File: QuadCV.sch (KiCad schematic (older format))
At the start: 22 parts, among them U8 MCP6004

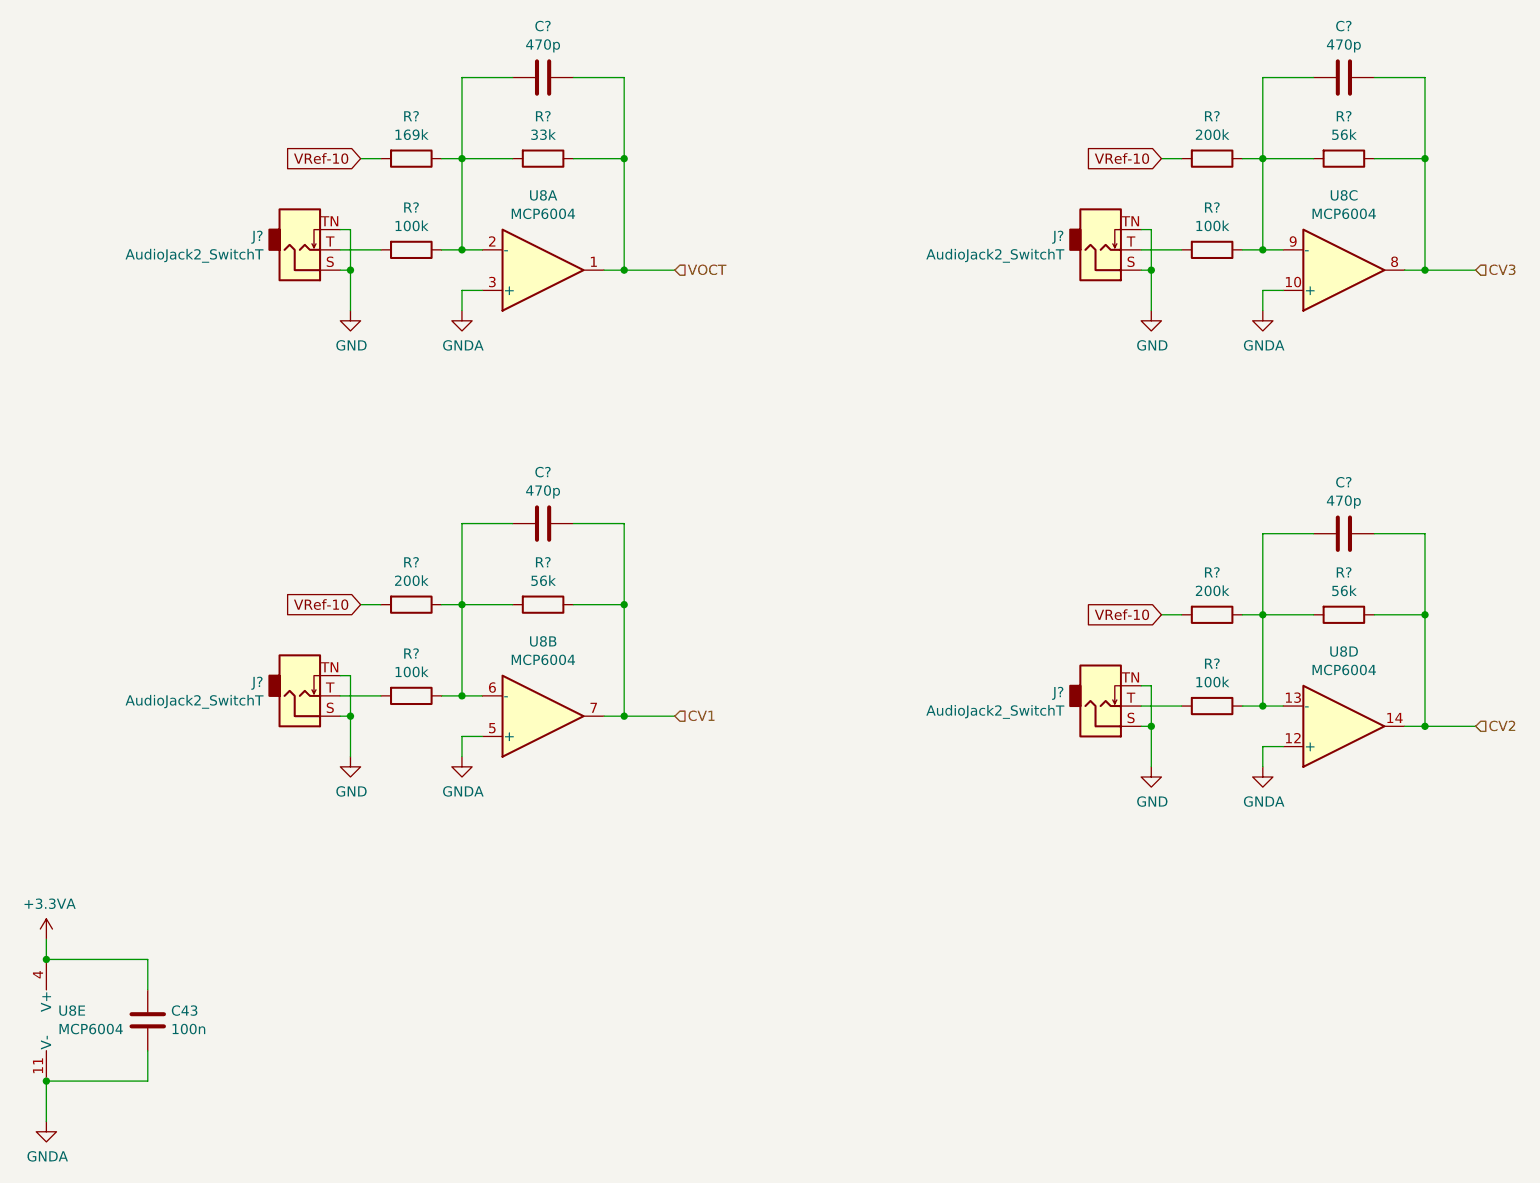
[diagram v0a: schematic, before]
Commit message: Added UI components.
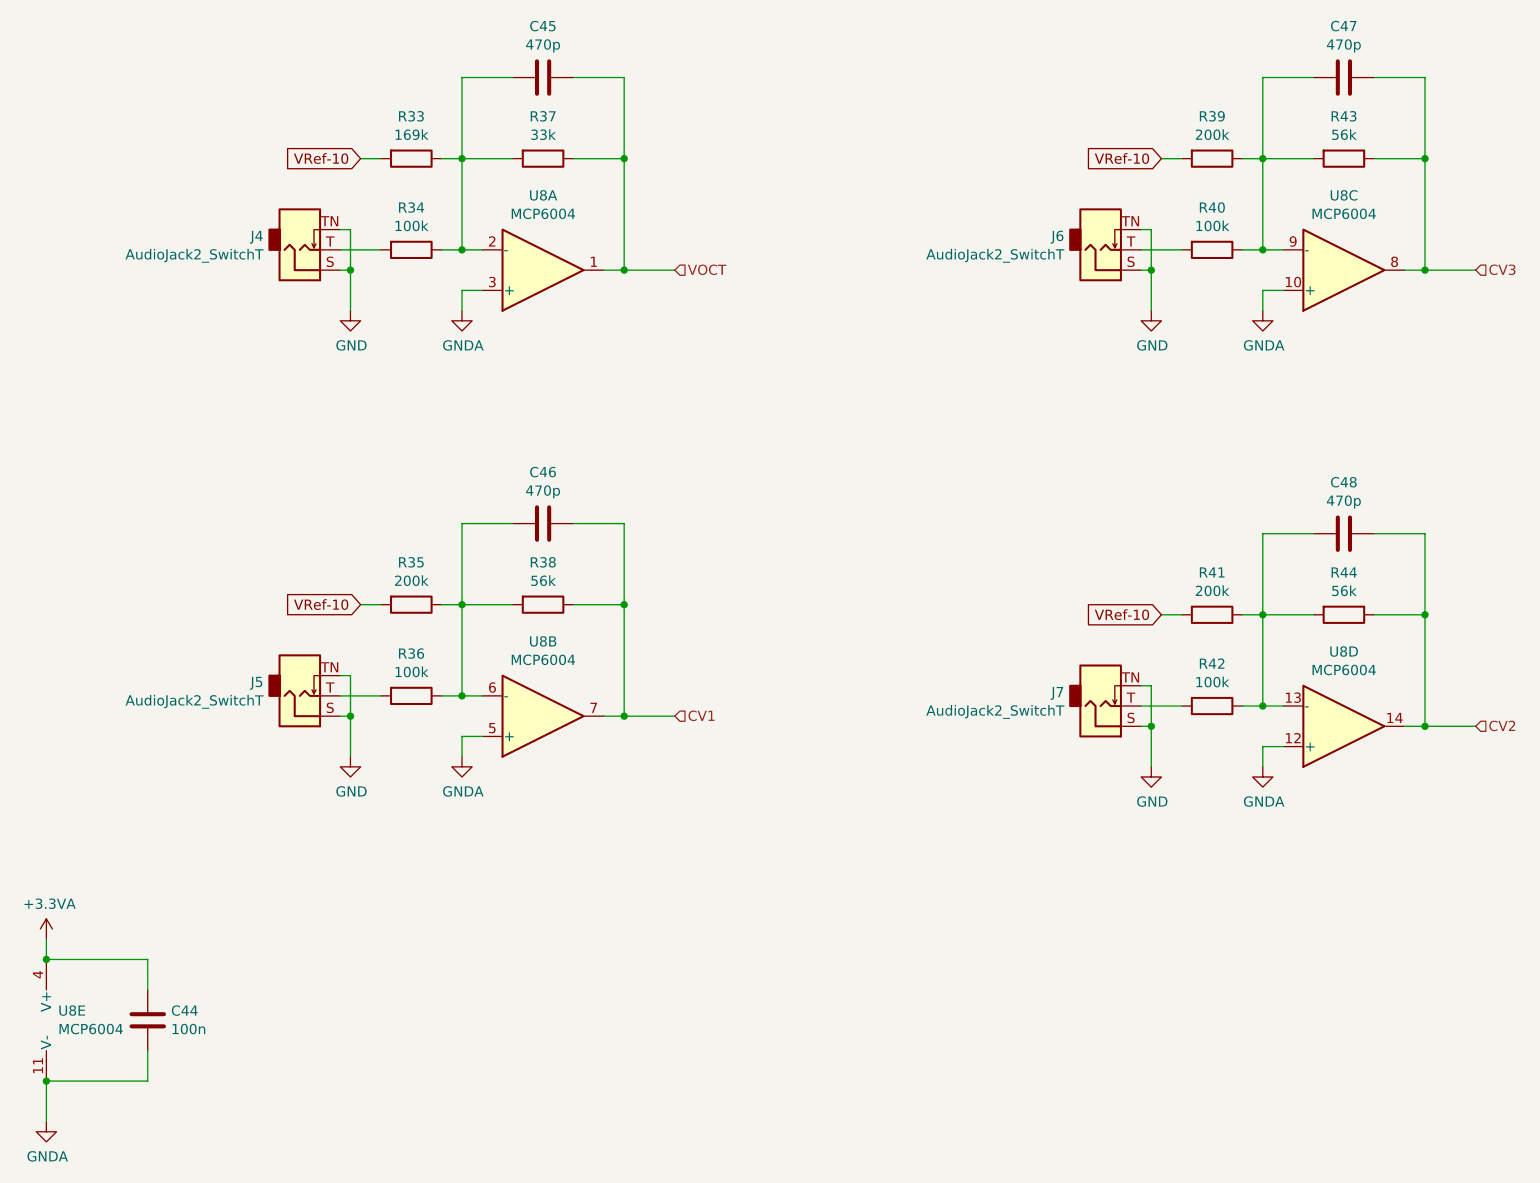
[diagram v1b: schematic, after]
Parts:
- gave numbers to parts that had none: 4
- renumbered C43 to C44, C44 to C45, C45 to C46, C46 to C47, C47 to C48, R27 to R33, R28 to R34, R29 to R35, R30 to R36, R31 to R37, R32 to R38, R33 to R39, R34 to R40, R35 to R41, R36 to R42, R37 to R43, R38 to R44

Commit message: Moved codec to audio module.
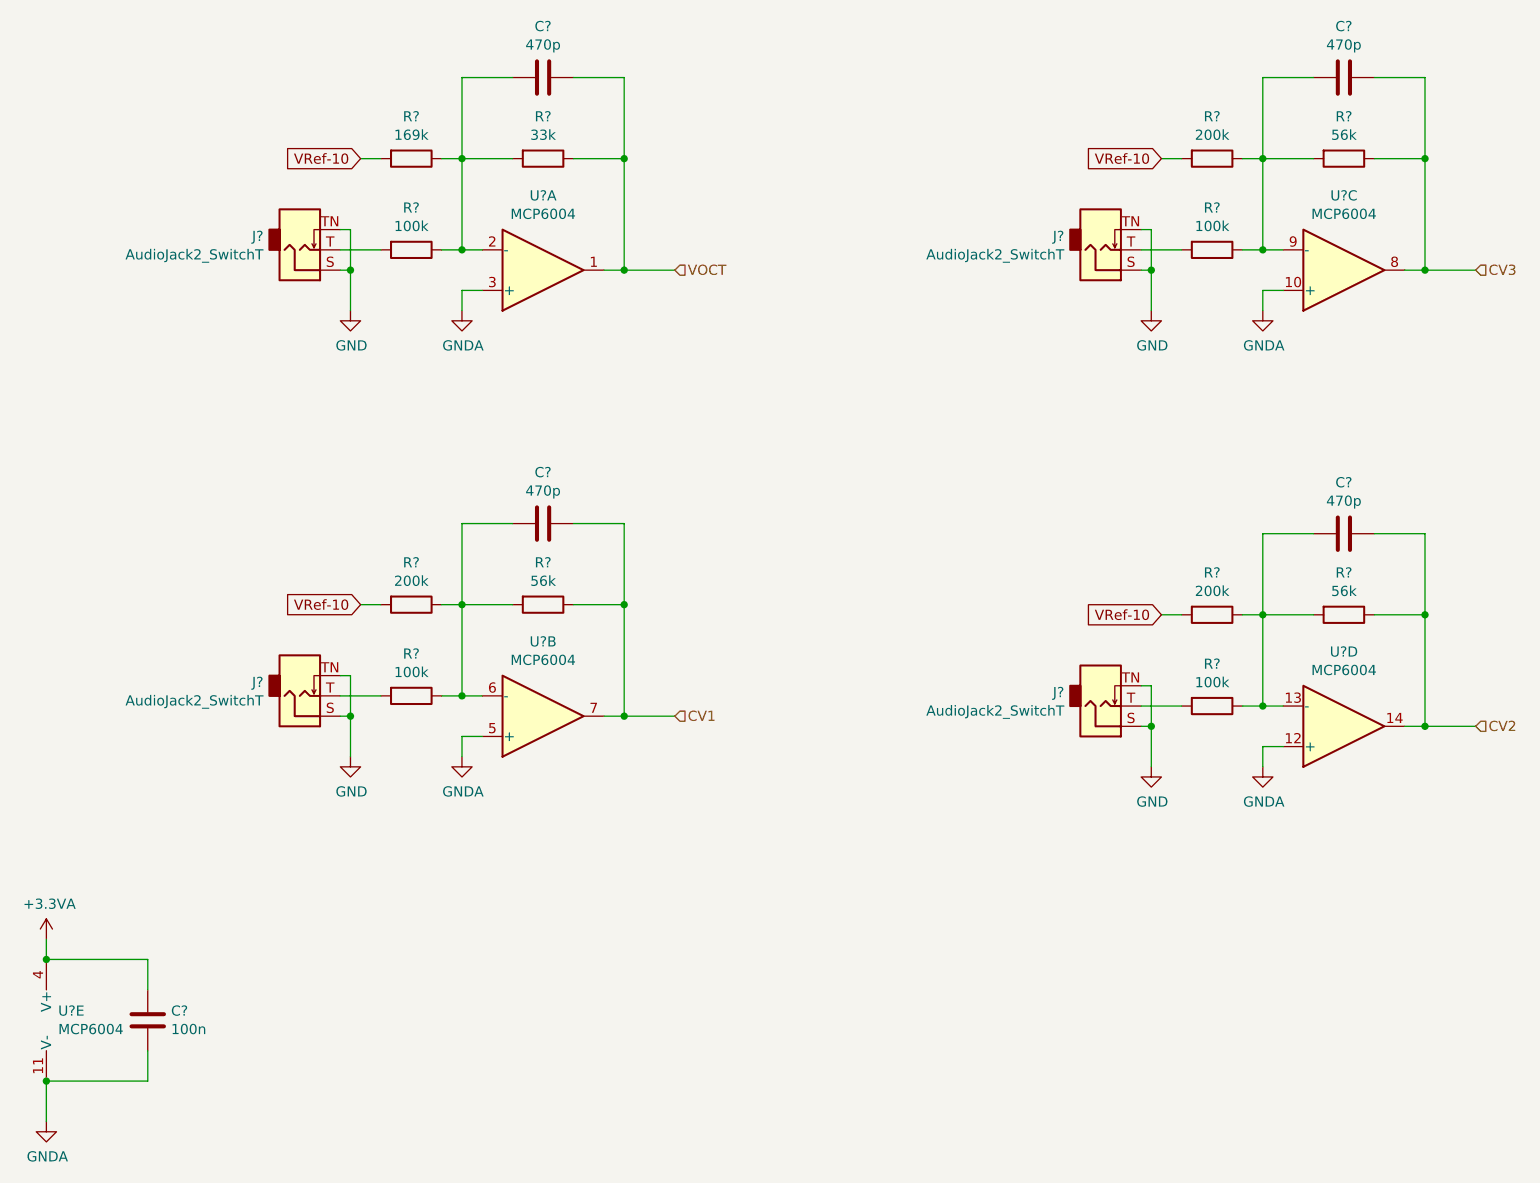
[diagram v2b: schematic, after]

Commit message: Re-annotation.
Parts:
- renumbered C44 to C27, C45 to C28, C46 to C29, C47 to C30, C48 to C31, R33 to R13, R34 to R14, R35 to R15, R36 to R16, R37 to R17, R38 to R18, R39 to R19, R40 to R20, R41 to R21, R42 to R22, R43 to R23, R44 to R24, U8 to U6

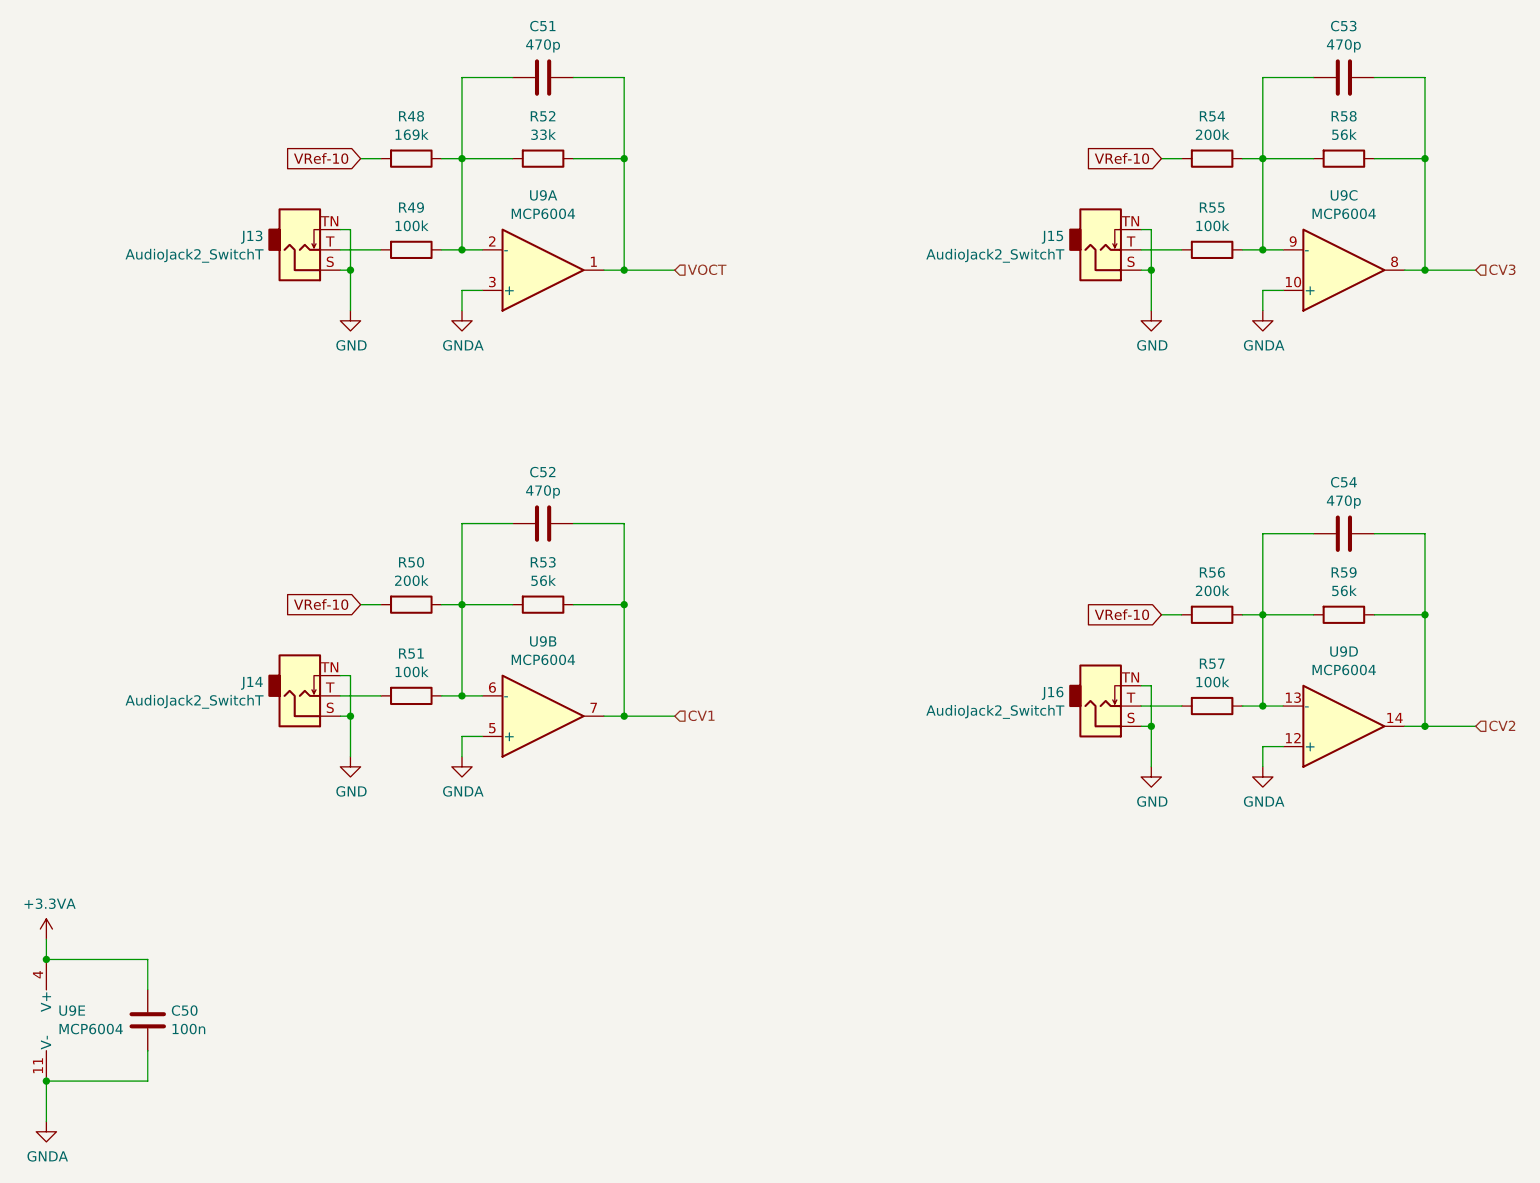
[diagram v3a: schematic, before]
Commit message: Assigned pins and cleared schema rules.
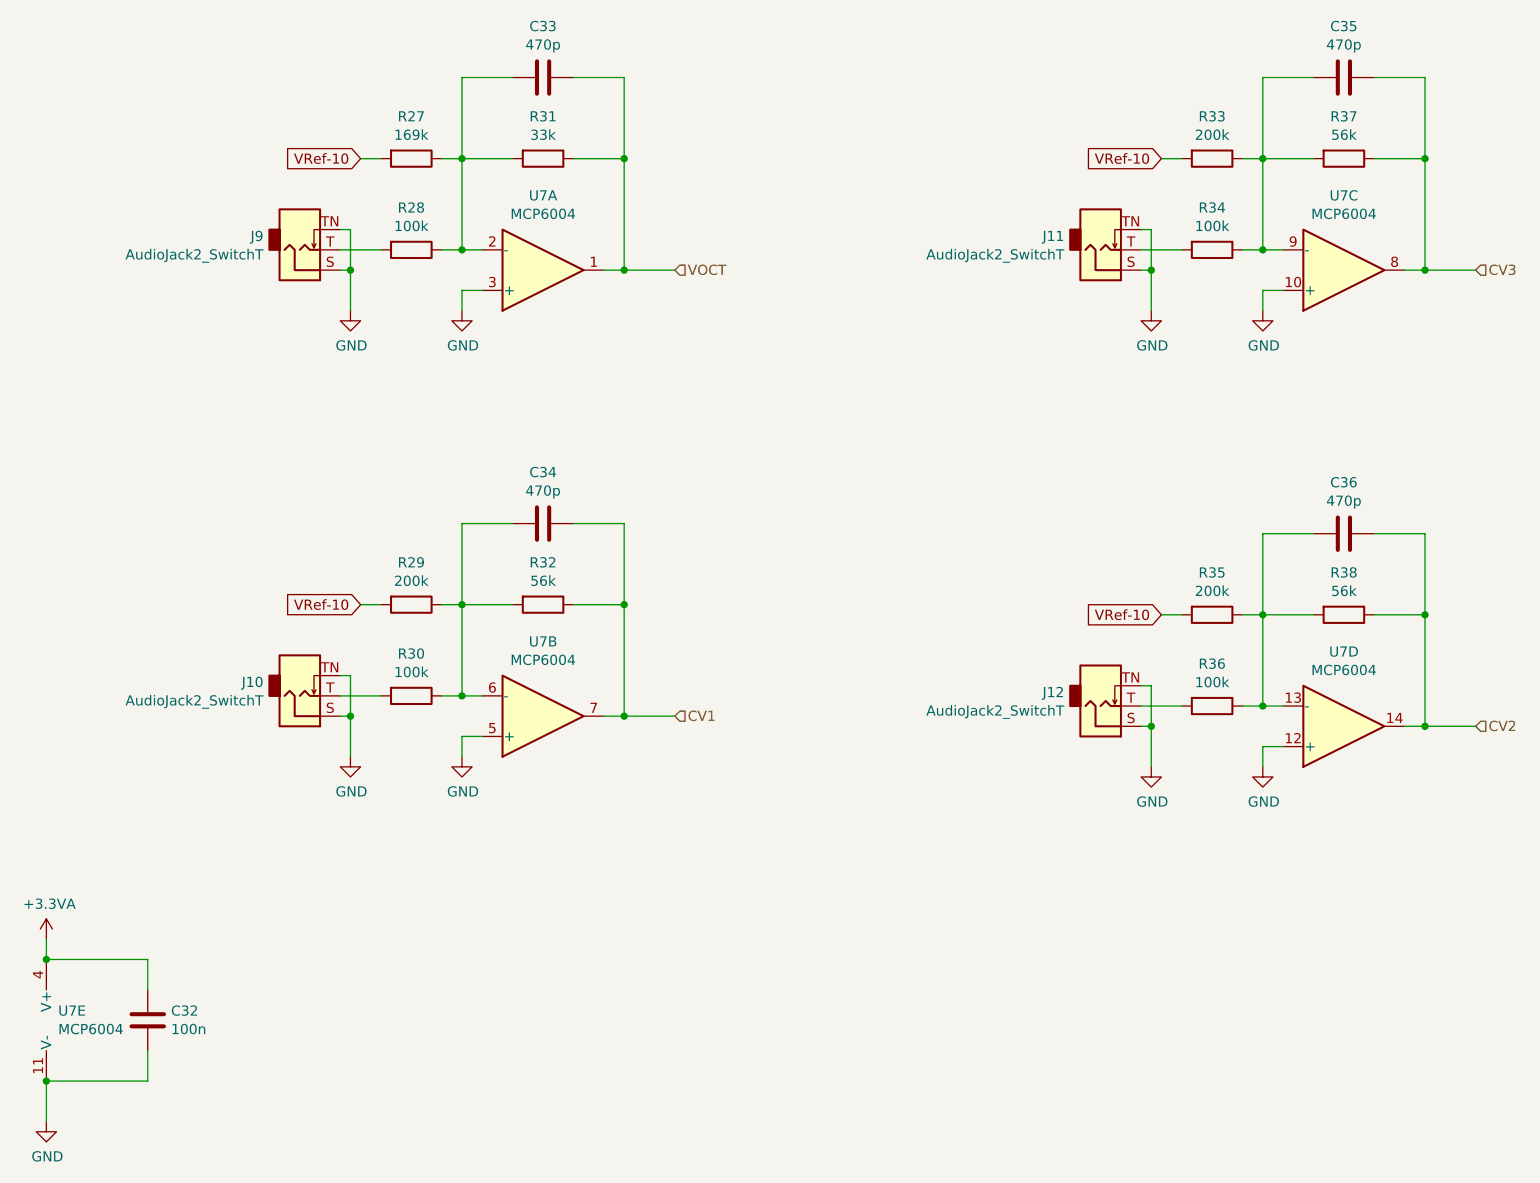
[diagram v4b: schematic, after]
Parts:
- C27: footprint Capacitor_SMD:C_0603_1608Metric -> Capacitor_SMD:C_0402_1005Metric
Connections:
- net GNDA is gone; now on net GND: C27.2, U6.10 (+), U6.11 (V-), U6.12 (+), U6.3 (+), U6.5 (+)
